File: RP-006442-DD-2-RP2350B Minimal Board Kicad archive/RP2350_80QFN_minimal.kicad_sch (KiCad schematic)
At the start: 49 parts, among them J1 USB_B_Micro, J2 Conn_02x26_Odd_Even, J3 Conn_02x26_Odd_Even, J4 SM03B-SRSS-TB, SW1 SW_Push, SW2 SW_Push, U1 RP2350_80QFN, U2 NCP1117-3.3_SOT223, U3 W25Q128JVS, U4 DNF, Y1 ABM8-272-T3

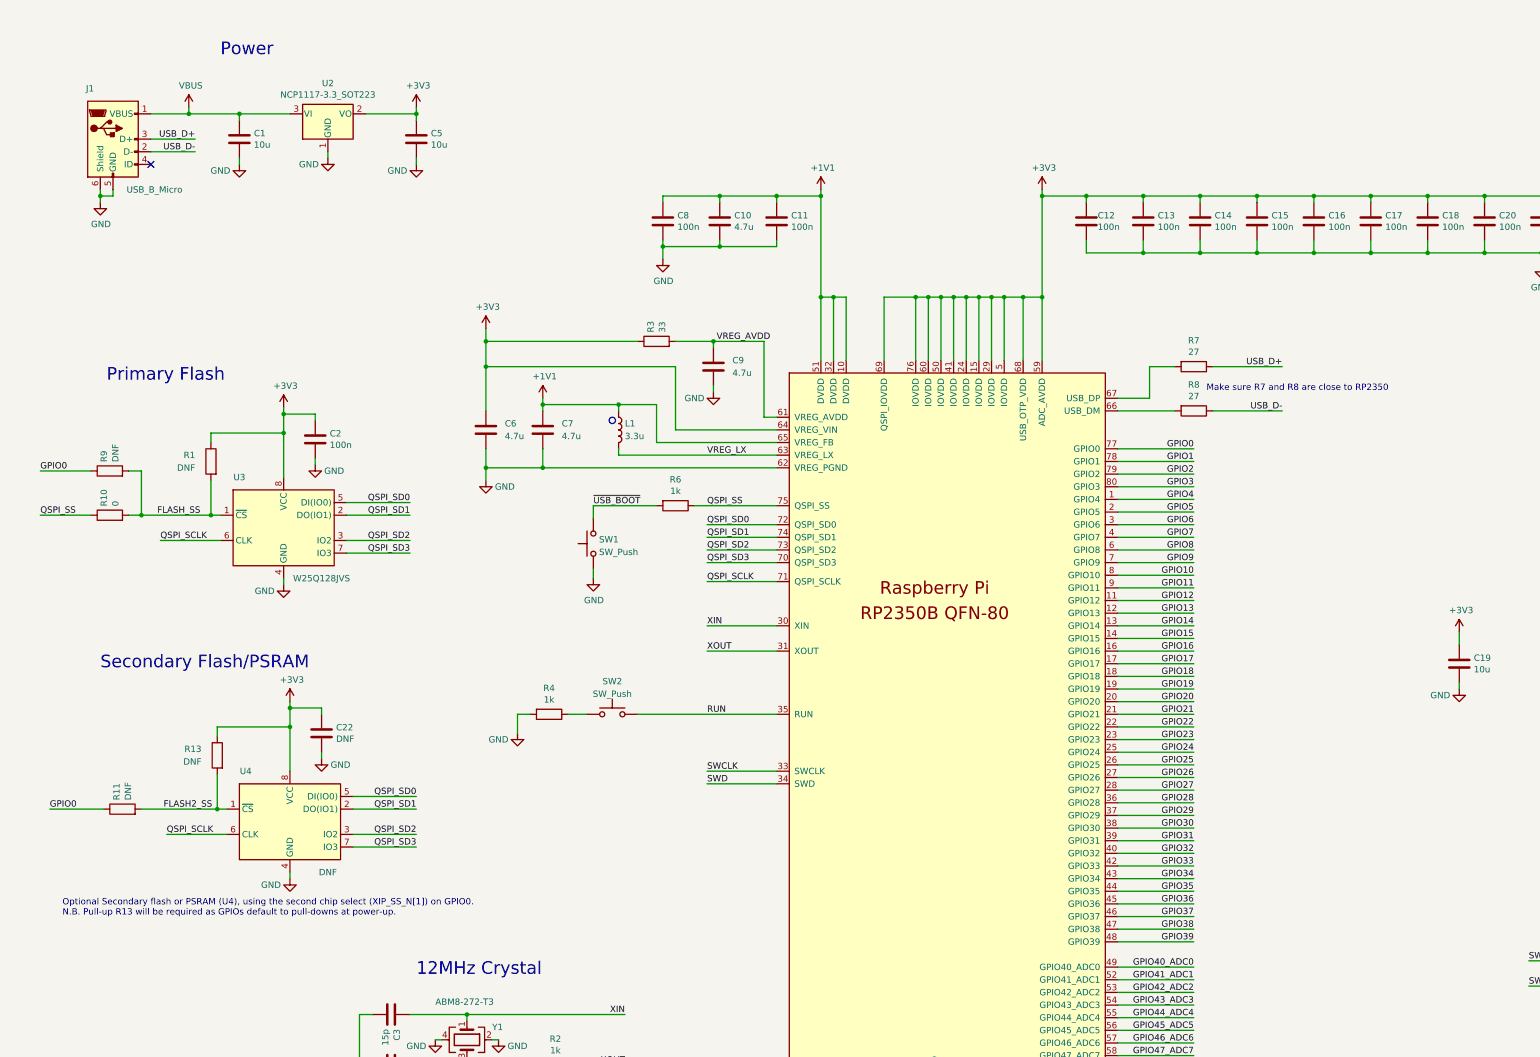
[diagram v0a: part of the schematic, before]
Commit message: Added circuit schematic for debugprobe
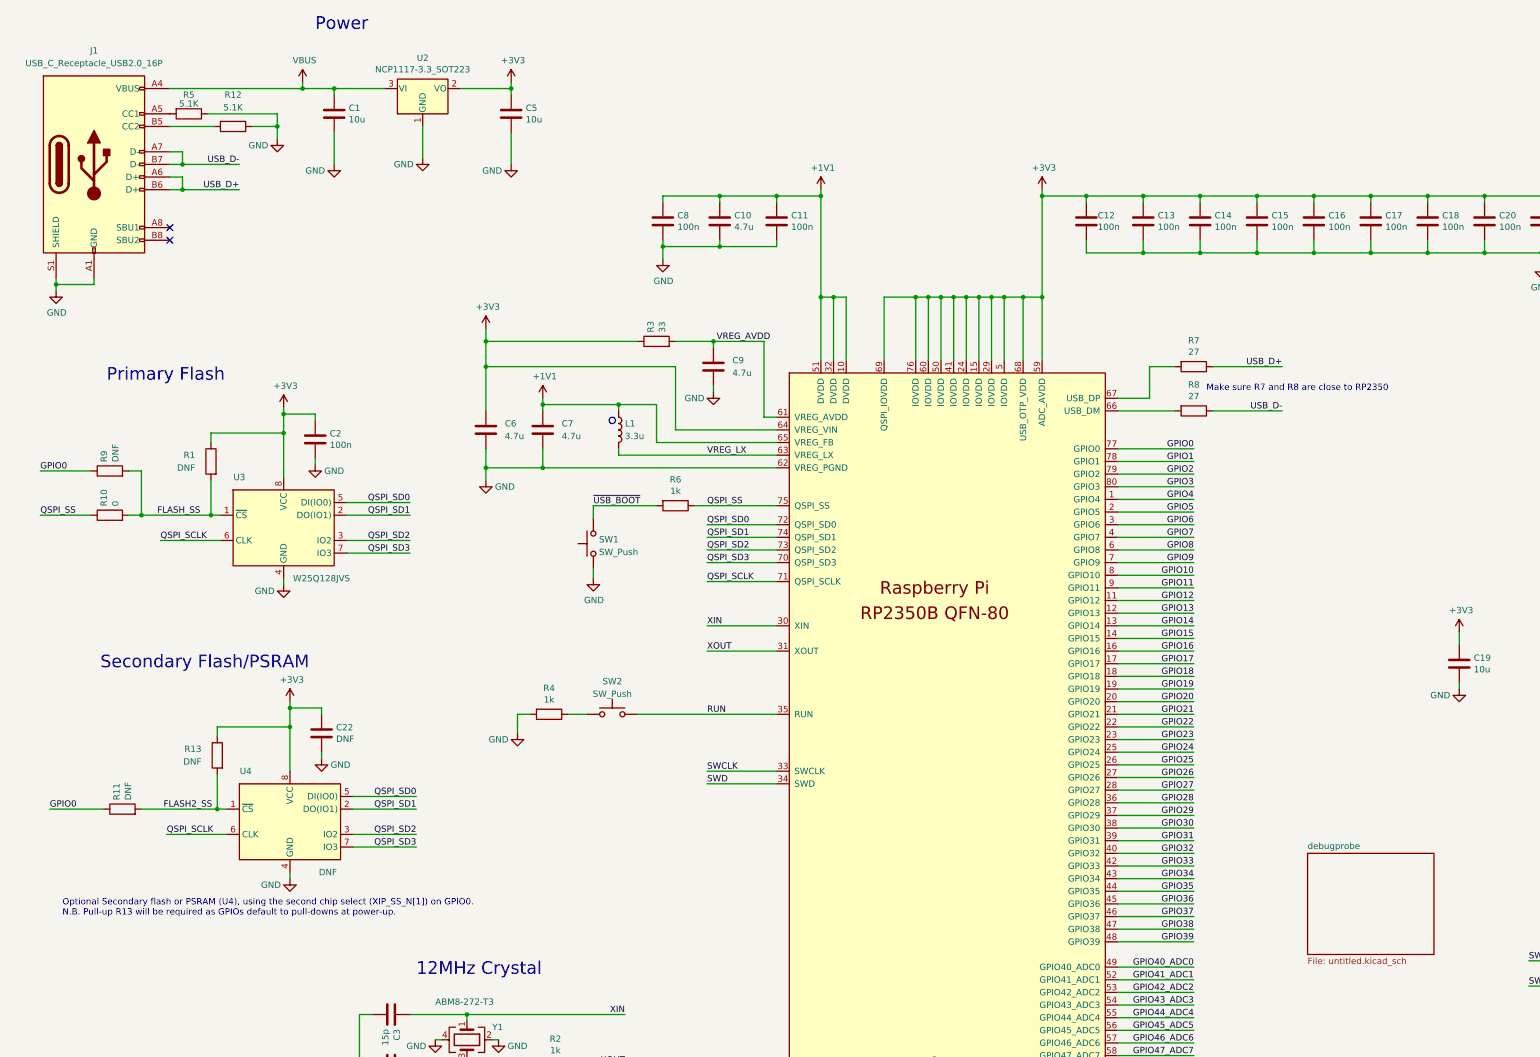
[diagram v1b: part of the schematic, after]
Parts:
- removed J1: USB_B_Micro, Connector_USB:USB_Micro-B_Amphenol_10103594-0001LF_Horizontal, symbol Connector:USB_B_Micro
- added J1: USB_C_Receptacle_USB2.0_16P, Connector_USB:USB_C_Receptacle_HRO_TYPE-C-31-M-12, symbol Connector:USB_C_Receptacle_USB2.0_16P
- added R12, R5: 5.1K, symbol Device:R
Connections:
- net GND: now also J1.A1 (GND), J1.A12 (GND), J1.B1 (GND), J1.B12 (GND), J1.S1 (SHIELD), R12.1, R5.1
- net USB_D+: now also J1.A6 (D+), J1.B6 (D+)
- net USB_D-: now also J1.A7 (D-), J1.B7 (D-)
- net VBUS: now also J1.A4 (VBUS), J1.A9 (VBUS), J1.B4 (VBUS), J1.B9 (VBUS)
- new net: J1.A5 (CC1), R5.2
- new net: J1.B5 (CC2), R12.2
- no-connect marks 1 -> 2
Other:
- added sheet debugprobe (untitled.kicad_sch)
- moved on the sheet: C1, C5, U2

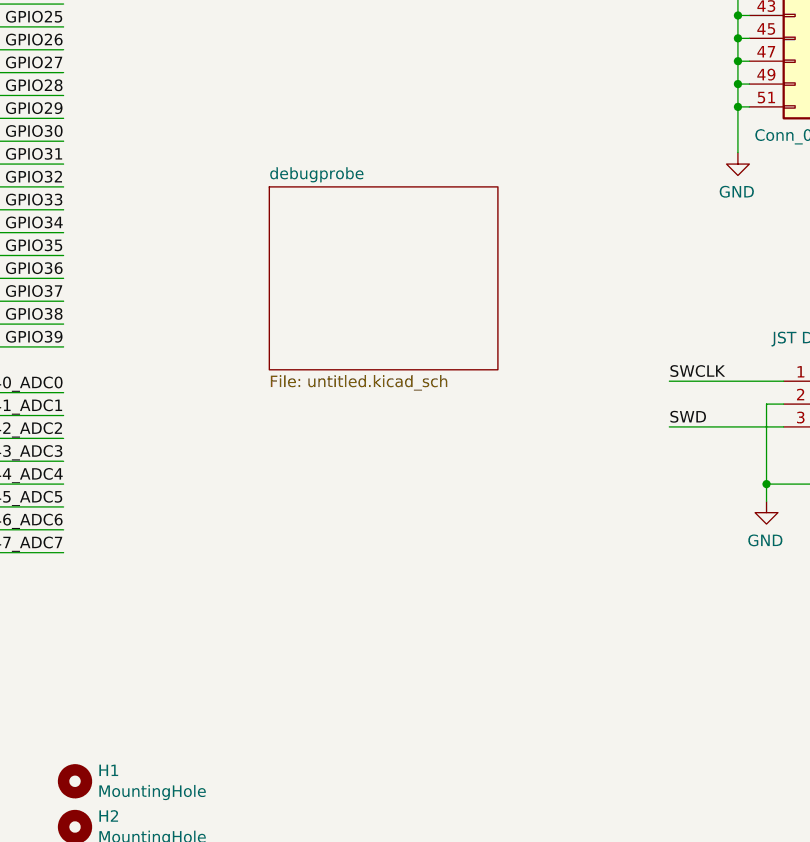
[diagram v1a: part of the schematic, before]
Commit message: Added hex displays schematic sheet
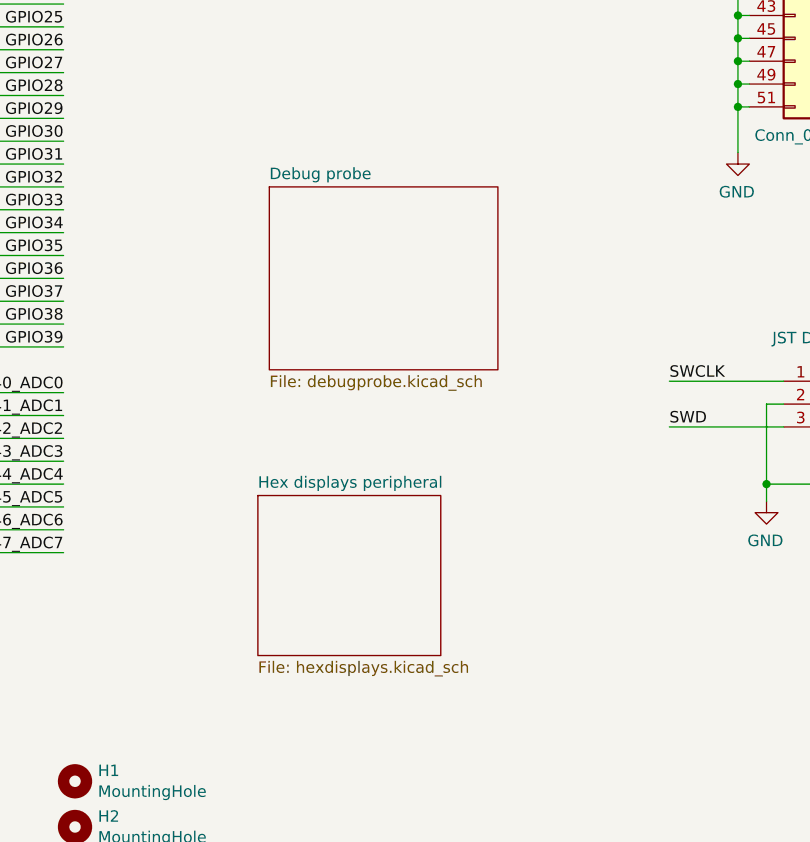
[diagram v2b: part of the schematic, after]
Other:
- sheet debugprobe renamed Debug probe
- added sheet Hex displays peripheral (hexdisplays.kicad_sch)
- sheet Debug probe: file untitled.kicad_sch -> debugprobe.kicad_sch
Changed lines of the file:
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@@
+	)
+	(sheet
+		(at 271.78 227.33)
+		(size 20.32 17.78)
+		(fields_autoplaced yes)
+		(stroke
+			(width 0.1524)
+			(type solid)
+		)
+		(fill
+			(color 0 0 0 0.0000)
+		)
+		(property "Sheetname" "Hex displays peripheral"
+			(at 271.78 226.6184 0)
+			(effects
+				(font
+					(size 1.27 1.27)
+				)
+				(justify left bottom)
+			)
+		)
+		(property "Sheetfile" "hexdisplays.kicad_sch"
+			(at 271.78 245.6946 0)
+			(effects
+				(font
+					(size 1.27 1.27)
+				)
+				(justify left top)
+			)
+		)
+		(instances
+			(project "RP2350_80QFN_minimal"
+				(path "/94683f5c-9cd9-448e-be96-9792537b5cb8"
+					(page "3")
+				)
+			)
+		)
 	)
 	(sheet
@@
 			(color 0 0 0 0.0000)
 		)
-		(property "Sheetname" "debugprobe"
+		(property "Sheetname" "Debug probe"
 			(at 273.05 192.3284 0)
 			(effects
@@
 			)
 		)
-		(property "Sheetfile" "untitled.kicad_sch"
+		(property "Sheetfile" "debugprobe.kicad_sch"
 			(at 273.05 213.9446 0)
 			(effects

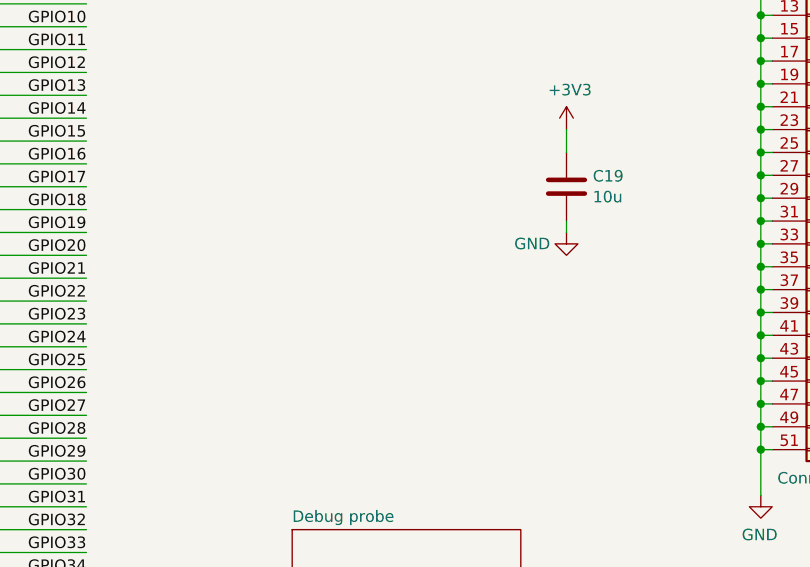
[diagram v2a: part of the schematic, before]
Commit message: added schematic page
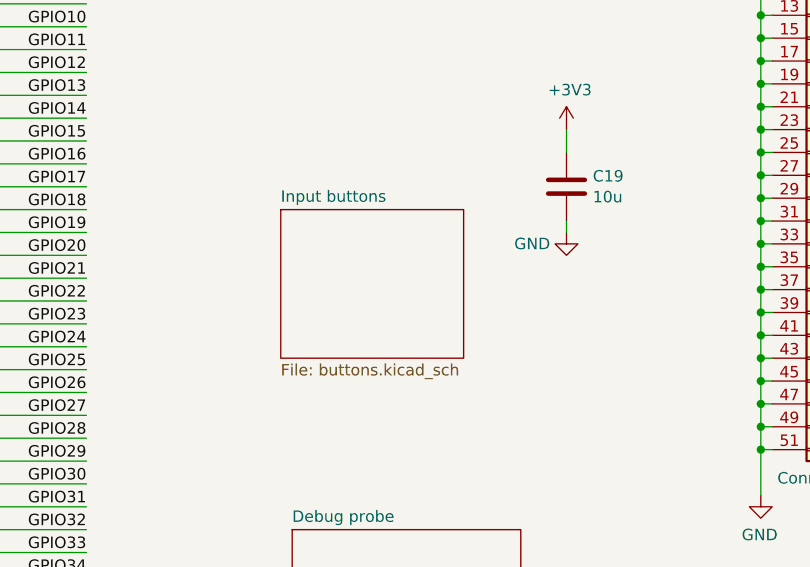
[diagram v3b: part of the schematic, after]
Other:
- added sheet Input buttons (buttons.kicad_sch)
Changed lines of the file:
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@@
+		)
+	)
+	(sheet
+		(at 271.78 157.48)
+		(size 20.32 16.51)
+		(fields_autoplaced yes)
+		(stroke
+			(width 0.1524)
+			(type solid)
+		)
+		(fill
+			(color 0 0 0 0.0000)
+		)
+		(property "Sheetname" "Input buttons"
+			(at 271.78 156.7684 0)
+			(effects
+				(font
+					(size 1.27 1.27)
+				)
+				(justify left bottom)
+			)
+		)
+		(property "Sheetfile" "buttons.kicad_sch"
+			(at 271.78 174.5746 0)
+			(effects
+				(font
+					(size 1.27 1.27)
+				)
+				(justify left top)
+			)
+		)
+		(instances
+			(project "RP2350_80QFN_minimal"
+				(path "/94683f5c-9cd9-448e-be96-9792537b5cb8"
+					(page "4")
+				)
+			)
 		)
 	)
